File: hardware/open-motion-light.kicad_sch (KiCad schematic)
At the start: 93 parts, among them J1 TYPE-C-31-M-12, Q1 2N7002, SW1 SW_Push, SW3 SSSS213800, U1 CN3058E, U2 VCNL4020-GS08, U3 MT9284BS6, U4 PIR223D-S0, U6 CH340X, U7 STM32L051K8Ux

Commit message: Hardware revision v1.1
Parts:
- D5, D6, D7, D9: LCSC C5252448 -> C5199848
- R11, R12: value 1k -> 10k; LCSC C11702 -> C25744
- U7: LCSC (none) -> C516778
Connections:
- net GND: now also C6.1; no longer C6.2
- net VCC: now also C6.2, R37.2; no longer C6.1, R37.1
- net at C12.2, C20.1, U2.5 (VDD): now also R37.1; no longer R37.2
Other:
- note added: "MCU input capacitance is 5pF TVS diode capacitance is 80pf At 4MΩ, T=340us"
- note removed: "MCU input capacitance is 5pF At 4MΩ, T=20us"
- moved on the sheet: R37
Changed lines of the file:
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@@
 	)
 	(junction
+		(at 264.16 160.02)
+		(diameter 0)
+		(color 0 0 0 0)
+	)
+	(junction
 		(at 88.9 20.32)
 		(diameter 0)
@@
 	)
 	(junction
+		(at 264.16 167.64)
+		(diameter 0)
+		(color 0 0 0 0)
+	)
+	(junction
 		(at 105.41 91.44)
 		(diameter 0)
@@
 	)
 	(junction
-		(at 264.16 167.64)
-		(diameter 0)
-		(color 0 0 0 0)
-	)
-	(junction
 		(at 49.53 160.02)
 		(diameter 0)
@@
 	)
 	(junction
-		(at 264.16 160.02)
-		(diameter 0)
-		(color 0 0 0 0)
-	)
-	(junction
 		(at 346.71 59.69)
 		(diameter 0)
@@
 	(wire
 		(pts
-			(xy 264.16 167.64) (xy 276.86 167.64)
-		)
-		(stroke
-			(width 0)
-			(type default)
-		)
-	)
-	(wire
-		(pts
 			(xy 49.53 181.61) (xy 49.53 180.34)
 		)
@@
 	(wire
 		(pts
+			(xy 264.16 167.64) (xy 276.86 167.64)
+		)
+		(stroke
+			(width 0)
+			(type default)
+		)
+	)
+	(wire
+		(pts
 			(xy 219.71 175.26) (xy 228.6 175.26)
 		)
@@
 	(polyline
 		(pts
-			(xy 73.66 138.43) (xy 73.66 196.85)
+			(xy 73.66 138.43) (xy 73.66 198.12)
 		)
 		(stroke
@@
 	(wire
 		(pts
+			(xy 264.16 160.02) (xy 276.86 160.02)
+		)
+		(stroke
+			(width 0)
+			(type default)
+		)
+	)
+	(wire
+		(pts
 			(xy 162.56 99.06) (xy 171.45 99.06)
 		)
@@
 	(polyline
 		(pts
-			(xy 73.66 196.85) (xy 13.97 196.85)
+			(xy 73.66 198.12) (xy 13.97 198.12)
 		)
 		(stroke
@@
 	(polyline
 		(pts
-			(xy 13.97 196.85) (xy 13.97 138.43)
+			(xy 13.97 198.12) (xy 13.97 138.43)
 		)
 		(stroke
@@
 	(wire
 		(pts
-			(xy 276.86 160.02) (xy 264.16 160.02)
-		)
-		(stroke
-			(width 0)
-			(type default)
-		)
-	)
-	(wire
-		(pts
-			(xy 264.16 160.02) (xy 251.46 160.02)
+			(xy 251.46 160.02) (xy 264.16 160.02)
 		)
 		(stroke
@@
 		)
 	)
-	(text "MCU input capacitance is 5pF\nAt 4MΩ, T=20us"
+	(text "MCU input capacitance is 5pF\nTVS diode capacitance is 80pf\nAt 4MΩ, T=340us"
 		(exclude_from_sim no)
 		(at 56.642 194.564 0)
@@
 			)
 		)
-		(property "LCSC" "C5252448"
+		(property "LCSC" "C5199848"
 			(at 36.83 184.15 90)
 			(effects
@@
 			)
 		)
-		(property "Value" "1k"
+		(property "Value" "10k"
 			(at 90.17 40.4438 90)
 			(effects
@@
 			)
 		)
-		(property "LCSC" "C11702"
+		(property "LCSC" "C25744"
 			(at 90.17 43.18 0)
 			(effects
@@
 			)
 		)
-		(property "LCSC" "C5252448"
+		(property "LCSC" "C5199848"
 			(at 49.53 163.83 90)
 			(effects
@@
 			)
 		)
-		(property "LCSC" "C5252448"
+		(property "LCSC" "C5199848"
 			(at 114.3 95.25 90)
 			(effects
@@
 			)
 		)
-		(property "Value" "1k"
+		(property "Value" "10k"
 			(at 22.86 32.8238 90)
 			(effects
@@
 			)
 		)
-		(property "LCSC" "C11702"
+		(property "LCSC" "C25744"
 			(at 22.86 35.56 0)
 			(effects
@@
 		(lib_id "Device:C")
 		(at 264.16 163.83 0)
+		(mirror x)
 		(unit 1)
 		(exclude_from_sim no)
@@
 		(on_board yes)
 		(dnp no)
-		(fields_autoplaced yes)
 		(property "Reference" "C6"
-			(at 267.081 162.6178 0)
+			(at 267.081 165.0422 0)
 			(effects
 				(font
@@
 		)
 		(property "Value" "100nF"
-			(at 267.081 165.0421 0)
+			(at 267.081 162.6179 0)
 			(effects
 				(font
@@
 		)
 		(property "Footprint" "Capacitor_SMD:C_0402_1005Metric"
-			(at 265.1252 167.64 0)
+			(at 265.1252 160.02 0)
 			(effects
 				(font
@@
 			)
 		)
+		(property "LCSC" "C516778"
+			(at 241.3 195.58 0)
+			(effects
+				(font
+					(size 1.27 1.27)
+				)
+				(hide yes)
+			)
+		)
 		(pin "8"
 		)
@@
 			)
 		)
-		(property "LCSC" "C5252448"
+		(property "LCSC" "C5199848"
 			(at 130.81 243.84 90)
 			(effects
@@
 	(symbol
 		(lib_id "Device:R")
-		(at 21.59 218.44 90)
+		(at 21.59 218.44 270)
+		(mirror x)
 		(unit 1)
 		(exclude_from_sim no)
@@
 		(on_board yes)
 		(dnp no)
-		(fields_autoplaced yes)
 		(property "Reference" "R37"
 			(at 21.59 213.2795 90)

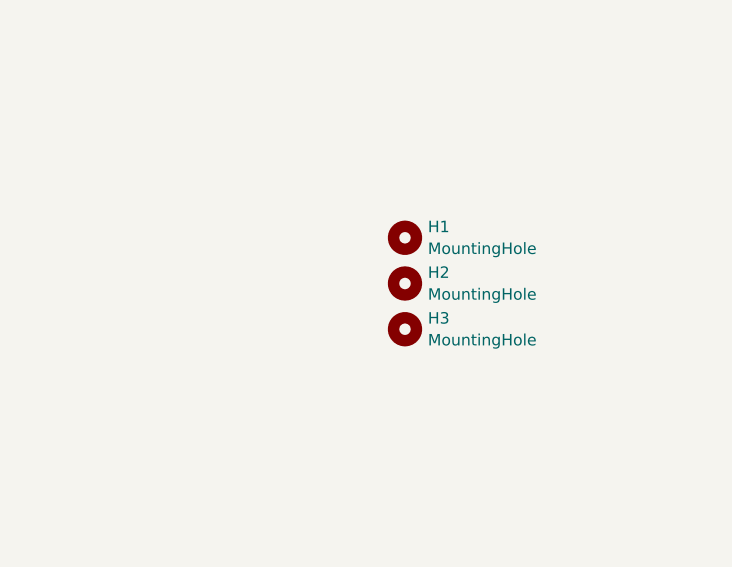
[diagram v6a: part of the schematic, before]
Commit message: Add JLC part number for light sensor
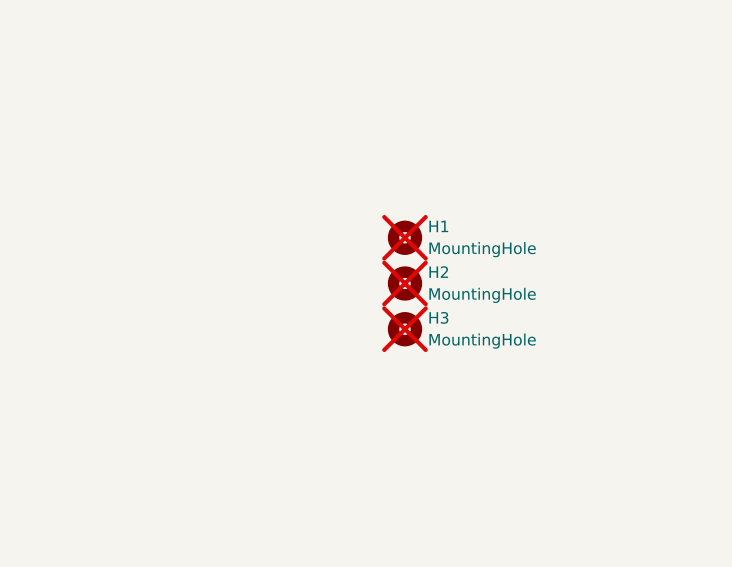
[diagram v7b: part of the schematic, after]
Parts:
- H1, H2, H3: now not fitted
- U2: LCSC (none) -> C511034
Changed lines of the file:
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@@
 		(in_bom no)
 		(on_board yes)
-		(dnp no)
+		(dnp yes)
 		(fields_autoplaced yes)
 		(property "Reference" "H1"
@@
 		(in_bom no)
 		(on_board yes)
-		(dnp no)
+		(dnp yes)
 		(fields_autoplaced yes)
 		(property "Reference" "H2"
@@
 			)
 		)
+		(property "LCSC" "C511034"
+			(at 50.8 254 0)
+			(effects
+				(font
+					(size 1.27 1.27)
+				)
+				(hide yes)
+			)
+		)
 		(pin "6"
 		)
@@
 		(in_bom no)
 		(on_board yes)
-		(dnp no)
+		(dnp yes)
 		(fields_autoplaced yes)
 		(property "Reference" "H3"

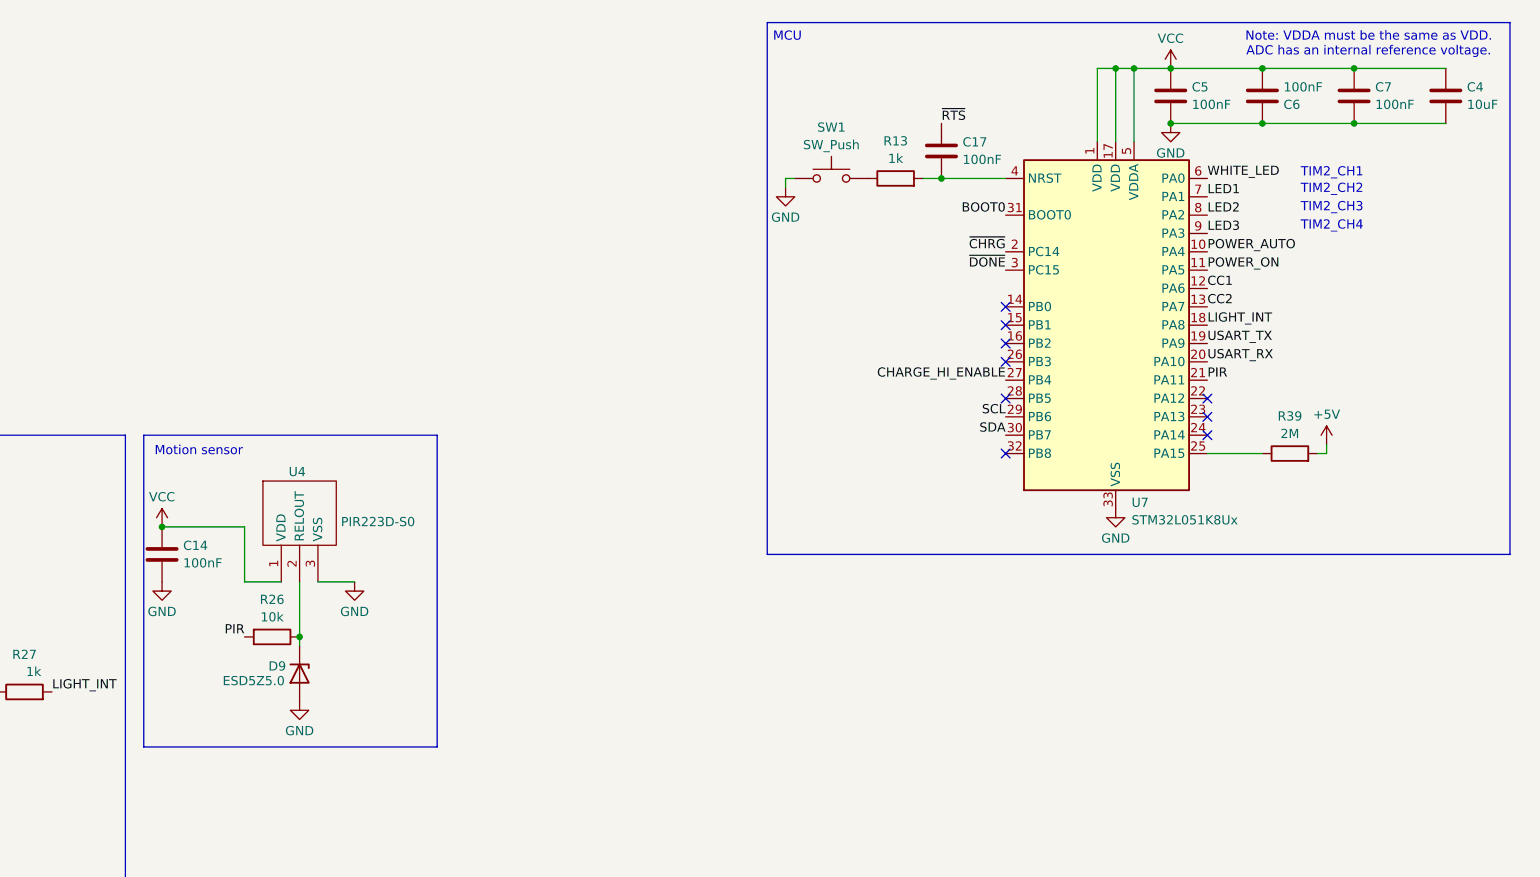
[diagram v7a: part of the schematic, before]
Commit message: Start updating schematic for v1.2
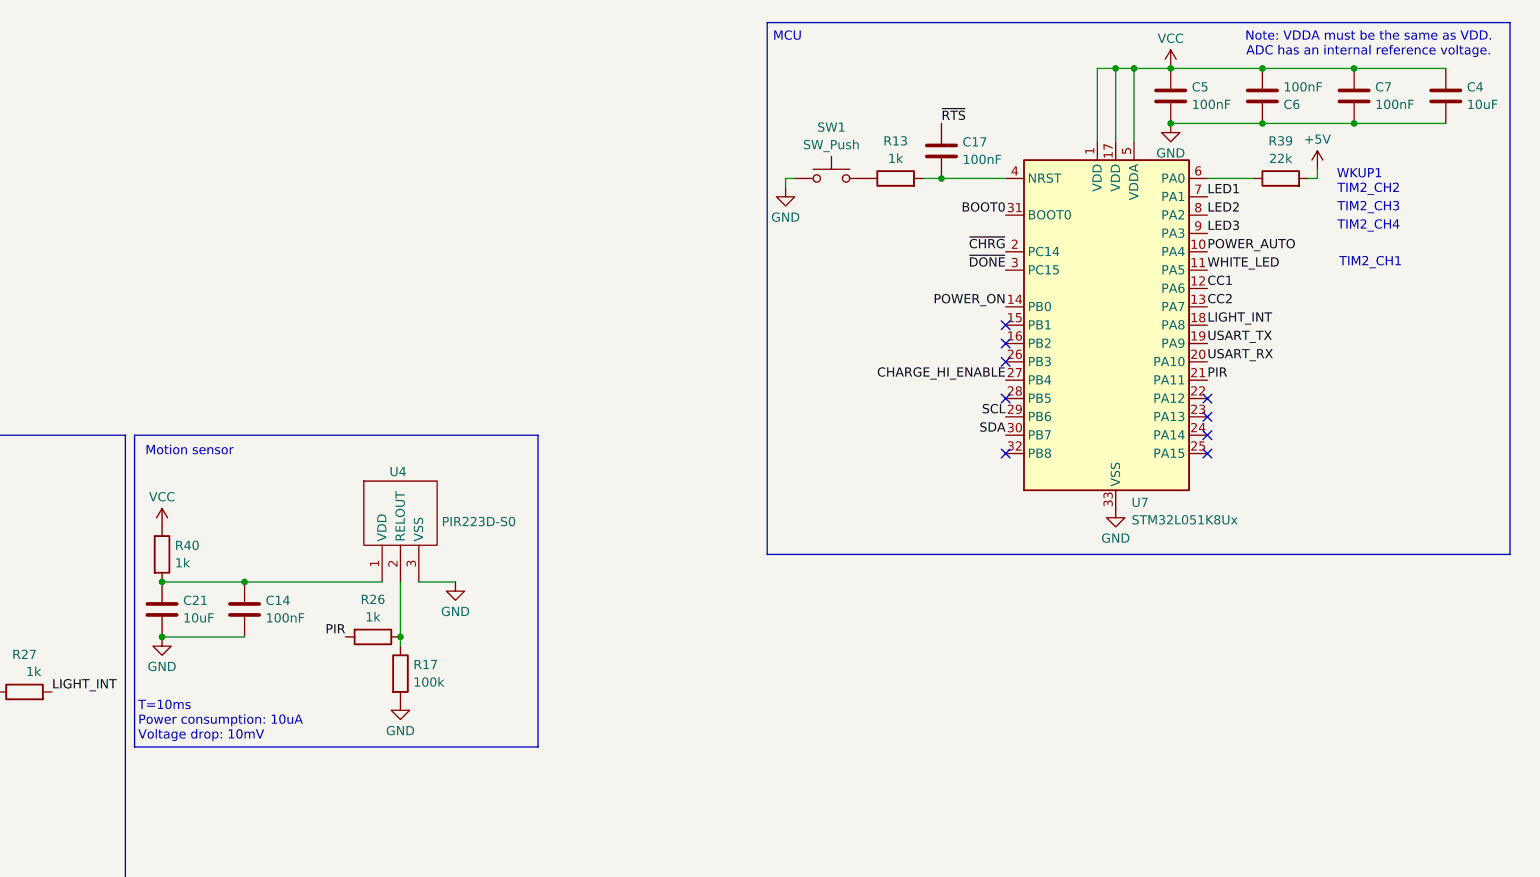
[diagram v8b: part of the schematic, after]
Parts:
- removed D9: ESD5Z5.0, Diode_SMD:D_SOD-523, symbol Diode:ESD5Zxx
- added C21: 10uF, Capacitor_SMD:C_0603_1608Metric, symbol Device:C
- added R17: 100k, Resistor_SMD:R_0402_1005Metric, symbol Device:R
- added R40: 1k, Resistor_SMD:R_0402_1005Metric, symbol Device:R
- R26: value 10k -> 1k; LCSC C25744 -> C11702
- R27, R8, R9: value 1k -> 1k
- R39: value 2M -> 22k; LCSC C22976 -> C25768
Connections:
- net GND: now also C21.2, R17.2
- net POWER_ON: now also U7.14 (PB0); no longer U7.11 (PA5)
- net VCC: now also R40.1; no longer C14.1, U4.1 (VDD)
- net WHITE_LED: now also U7.11 (PA5); no longer U7.6 (PA0)
- net at R39.1: now also U7.6 (PA0); no longer U7.25 (PA15)
- net at R26.1, U4.2 (RELOUT): now also R17.1
- new net: C14.1, C21.1, R40.2, U4.1 (VDD)
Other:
- note added: "T=10ms Power consumption: 10uA Voltage drop: 10mV"
- note added: "WKUP1"
- moved on the sheet: C14, R26, R39, U4
